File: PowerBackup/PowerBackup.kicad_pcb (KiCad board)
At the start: 4 copper layers, 40 x 41 mm, 3 parts

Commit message: Did some initial board layout
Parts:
- added C1: 1u, Capacitor_SMD:C_0805_2012Metric, F.Cu at (141.8, 115.0)
- added C10: 1u, Capacitor_SMD:C_0805_2012Metric, F.Cu at (125.0, 108.7)
- added C2: 1u, Capacitor_SMD:C_0805_2012Metric, F.Cu at (141.8, 113.0)
- added C3: 1u, Capacitor_SMD:C_0805_2012Metric, F.Cu at (141.8, 110.0)
- added C4: 1u, Capacitor_SMD:C_0805_2012Metric, F.Cu at (141.8, 107.5)
- added C5: 1u, Capacitor_SMD:C_0805_2012Metric, F.Cu at (141.8, 105.0)
- added C6: 1u, Capacitor_SMD:C_0805_2012Metric, F.Cu at (141.8, 102.8)
- added C7: 1u, Capacitor_SMD:C_0805_2012Metric, F.Cu at (141.8, 100.5)
- added C8: 10u, Capacitor_SMD:C_0805_2012Metric, F.Cu at (138.8, 105.5)
- added C9: 4.7u, Capacitor_SMD:C_0805_2012Metric, F.Cu at (136.5, 105.5)
- added D1: MBRB2515L, Package_TO_SOT_SMD:TO-263-2, F.Cu at (134.3, 89.0)
- added D2: MBRB2515L, Package_TO_SOT_SMD:TO-263-2, F.Cu at (119.4, 101.0)
- added J1: Conn_01x02_Female, Connector_JST:JST_XH_B2B-XH-A_1x02_P2.50mm_Vertical, B.Cu at (138.2, 79.8)
- added J2: Conn_01x07_Male, Connector_JST:JST_XH_B7B-XH-A_1x07_P2.50mm_Vertical, F.Cu at (147.6, 100.0)
- added J4: Conn_01x05_Female, Connector_PinHeader_1.00mm:PinHeader_1x05_P1.00mm_Vertical_SMD_Pin1Left, F.Cu at (131.8, 106.4)
- added J6: Conn_01x02_Female, Connector_JST:JST_XH_B2B-XH-A_1x02_P2.50mm_Vertical, F.Cu at (146.5, 92.5)
- added J7: Conn_01x02_Male, Connector_JST:JST_XH_B2B-XH-A_1x02_P2.50mm_Vertical, F.Cu at (114.1, 92.2)
- added Q1: ZXTP25040DFH, Package_TO_SOT_SMD:SOT-23, F.Cu at (137.2, 101.6)
- added R1: 100, Resistor_SMD:R_0805_2012Metric, B.Cu at (144.2, 100.0)
- added R10: 0.001, Resistor_SMD:R_0805_2012Metric, F.Cu at (135.0, 113.2)
- added R11: 0, Resistor_SMD:R_0805_2012Metric, F.Cu at (134.8, 98.8)
- added R12: 1k, Resistor_SMD:R_0805_2012Metric, F.Cu at (133.6, 110.5)
- added R13: 4k7, Resistor_SMD:R_0805_2012Metric, F.Cu at (133.6, 102.8)
- added R14: 200, Resistor_SMD:R_0805_2012Metric, B.Cu at (131.0, 105.6)
- added R15: 4k7, Resistor_SMD:R_0805_2012Metric, F.Cu at (133.6, 100.8)
- added R16: 0, Resistor_SMD:R_0805_2012Metric, F.Cu at (136.4, 96.8)
- added R17: 0, Resistor_SMD:R_0805_2012Metric, F.Cu at (139.8, 95.8)
- added R2: 100, Resistor_SMD:R_0805_2012Metric, B.Cu at (144.4, 104.8)
- added R3: 100, Resistor_SMD:R_0805_2012Metric, B.Cu at (144.4, 109.9)
- added R4: 100, Resistor_SMD:R_0805_2012Metric, B.Cu at (144.4, 115.0)
- added R5: 100, Resistor_SMD:R_0805_2012Metric, B.Cu at (144.4, 107.1)
- added R6: 100, Resistor_SMD:R_0805_2012Metric, B.Cu at (144.4, 102.3)
- added R7: 100, Resistor_SMD:R_0805_2012Metric, B.Cu at (144.4, 112.4)
- added R8: 100, Resistor_SMD:R_0805_2012Metric, F.Cu at (138.2, 98.8)
- added R9: 1k, Resistor_SMD:R_0805_2012Metric, F.Cu at (136.1, 110.5)
- added TH1: Thermistor_NTC, Resistor_SMD:R_0805_2012Metric, F.Cu at (128.8, 108.4)
- added U1: BQ76925RGET, Package_DFN_QFN:HVQFN-24-1EP_4x4mm_P0.5mm_EP2.5x2.5mm, B.Cu at (136.5, 105.2)
- H1, H2, H3: value MountingHole_3.2mm_M3_Pad -> MountingHole_Pad; footprint MountingHole:MountingHole_3.2mm_M3_Pad -> MountingHole:MountingHole_2.7mm_M2.5_Pad
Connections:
- H1 pad 1: (no net) -> GND
- H2 pad 1: (no net) -> GND
- H3 pad 1: (no net) -> GND
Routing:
- net Net-(J3-Pad3): track 0.00 -> 16.6 mm, vias 0 -> 1
- net Net-(C7-Pad1): track 0.00 -> 12.9 mm, vias 0 -> 1
- net Net-(C1-Pad1): track 0.00 -> 12.4 mm, vias 0 -> 1
- net Net-(J5-Pad4): track 0.00 -> 10.9 mm
- net Net-(C2-Pad1): track 0.00 -> 10.9 mm, vias 0 -> 1
- net Net-(J3-Pad4): track 0.00 -> 10.5 mm, vias 0 -> 1
- net Net-(C8-Pad1): track 0.00 -> 9.98 mm, vias 0 -> 1
- net Net-(R11-Pad1): track 0.00 -> 9.76 mm, vias 0 -> 2
- net Net-(C6-Pad1): track 0.00 -> 9.17 mm, vias 0 -> 1
- net Net-(J5-Pad3): track 0.00 -> 8.93 mm
- net Net-(C3-Pad1): track 0.00 -> 8.46 mm, vias 0 -> 1
- net Net-(C5-Pad1): track 0.00 -> 7.85 mm, vias 0 -> 1
- net Net-(J4-Pad2): track 0.00 -> 7.33 mm, vias 0 -> 1
- net Net-(C4-Pad1): track 0.00 -> 6.65 mm, vias 0 -> 1
- net Net-(J4-Pad5): track 0.00 -> 6.32 mm, vias 0 -> 1
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- added copper zone on F.Cu, net +3V3
- added copper zone on F.Cu, net +9V
- added copper zone on F.Cu, net +9VA
- added copper zone on F.Cu, net /Backup/VBAT
- added copper zone on F.Cu, net GND
- added copper zone on In1.Cu, net GND

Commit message: Trying things
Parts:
- added J10: Conn_01x02_Female, Connector_JST:JST_XH_B2B-XH-A_1x02_P2.50mm_Vertical, F.Cu at (116.1, 115.1)
- added J8: Conn_01x02_Female, Connector_JST:JST_XH_B2B-XH-A_1x02_P2.50mm_Vertical, F.Cu at (113.5, 107.9)
- added J9: Conn_01x02_Female, Connector_JST:JST_XH_B2B-XH-A_1x02_P2.50mm_Vertical, F.Cu at (113.5, 91.4)
- D1, D2: value MBRB2515L -> SB2060TA; footprint Package_TO_SOT_SMD:TO-263-2 -> Diode_THT:D_A-405_P5.08mm_Vertical_KathodeUp
- moved C10 24.9 mm to (135.4, 86.1), turned to 0 degrees
- moved D2 19.5 mm to (131.4, 85.6), turned to 180 degrees
- moved J7 18.0 mm to (127.2, 79.8), turned to 0 degrees
- moved D1 5.92 mm to (134.6, 83.1), turned to 0 degrees
- moved J6 2.57 mm to (147.6, 90.2), turned to -90 degrees
- moved J1 1.77 mm to (140.0, 80.0)
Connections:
- D1 pad 1: +9V -> +9VA
- D1 pad 2: +9VA -> +9V
- D2 pad 1: /Backup/VBAT -> +9VA
- D2 pad 2: +9VA -> /Backup/VBAT
- R10 pad 2: GNDD -> GND
- R12 pad 2: GNDD -> GND
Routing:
- net GND: track 3.61 -> 8.52 mm
- net Net-(J2-Pad4): track 0.00 -> 2.51 mm
- net Net-(J2-Pad1): track 0.00 -> 2.48 mm
- net Net-(J5-Pad4): track 10.9 -> 13.4 mm, vias 0 -> 1
- net Net-(J2-Pad2): track 0.20 -> 2.64 mm
- net Net-(J2-Pad3): track 0.00 -> 2.42 mm
- net Net-(J2-Pad5): track 0.03 -> 2.42 mm
- net Net-(J2-Pad6): track 0.03 -> 2.39 mm
- net GNDD: track 2.54 -> 1.39 mm, vias 0 -> 10
- added copper zone on F.Cu, net GNDD
- added copper zone on In2.Cu, net GNDD

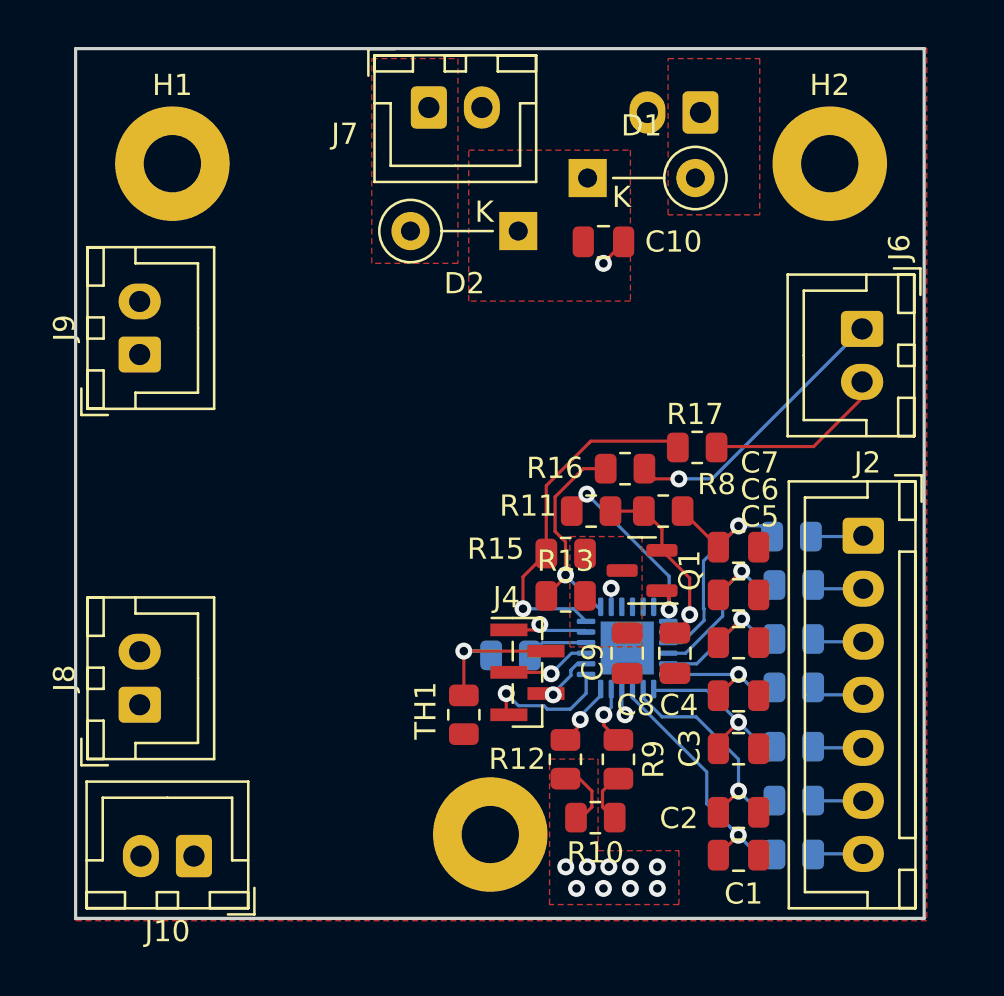
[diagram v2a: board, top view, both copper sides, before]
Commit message: Added 5V 9A buck converter
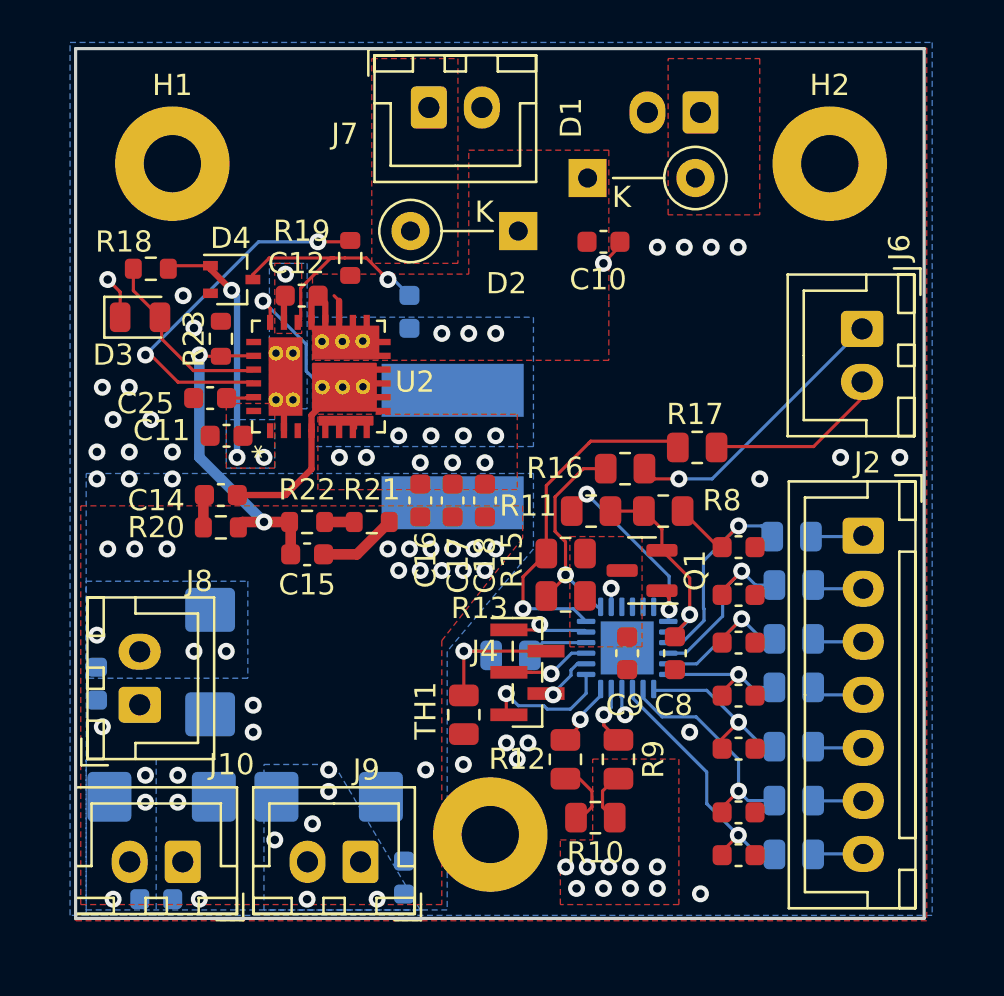
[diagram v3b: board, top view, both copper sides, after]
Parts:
- added C11: 2.2u, Capacitor_SMD:C_0603_1608Metric, F.Cu at (117.6, 95.2)
- added C12: 2.2u, Capacitor_SMD:C_0603_1608Metric, F.Cu at (121.2, 88.6)
- added C13: 0.1u, Capacitor_SMD:C_0603_1608Metric, B.Cu at (126.2, 89.4)
- added C14: 0.1u, Capacitor_SMD:C_0603_1608Metric, F.Cu at (117.3, 98.0)
- added C15: 0.1u, Capacitor_SMD:C_0603_1608Metric, F.Cu at (121.4, 100.8)
- added C16: 0.1u, Capacitor_SMD:C_0603_1608Metric, F.Cu at (126.7, 98.3)
- added C17: 1u, Capacitor_SMD:C_0603_1608Metric, F.Cu at (128.3, 98.3)
- added C18: 50u, Capacitor_SMD:C_0603_1608Metric, F.Cu at (129.8, 98.3)
- added C19: 4.7u, Capacitor_SMD:C_0603_1608Metric, B.Cu at (111.5, 106.9)
- added C20: 4.7u, Capacitor_SMD:C_0603_1608Metric, B.Cu at (114.3, 117.1)
- added C21: 4.7u, Capacitor_SMD:C_0603_1608Metric, B.Cu at (126.0, 116.1)
- added C22: 47u, Capacitor_Tantalum_SMD:CP_EIA-6032-15_Kemet-U, B.Cu at (116.8, 105.9)
- added C23: 47u, Capacitor_Tantalum_SMD:CP_EIA-6032-15_Kemet-U, B.Cu at (114.6, 112.3)
- added C24: 47u, Capacitor_Tantalum_SMD:CP_EIA-6032-15_Kemet-U, B.Cu at (122.4, 112.3)
- added C25: 2.2u, Capacitor_SMD:C_0603_1608Metric, F.Cu at (116.8, 93.5)
- added D3: LED_Small, LED_SMD:LED_0805_2012Metric, F.Cu at (113.5, 89.7)
- added D4: BAT54W, Package_TO_SOT_SMD:SOT-323_SC-70, F.Cu at (117.9, 87.9)
- added L1: 3.3u, Backup:Inductor_EXL1V0707-3R3-R, B.Cu at (128.3, 95.8)
- added R18: 1.5k, Resistor_SMD:R_0603_1608Metric, F.Cu at (114.0, 87.4)
- added R19: 10k, Resistor_SMD:R_0603_1608Metric, F.Cu at (123.4, 86.9)
- added R20: 19.6k, Resistor_SMD:R_0603_1608Metric, F.Cu at (117.3, 99.6)
- added R21: 7k5, Resistor_SMD:R_0603_1608Metric, F.Cu at (124.5, 99.3)
- added R22: 150k, Resistor_SMD:R_0603_1608Metric, F.Cu at (121.4, 99.3)
- added R23: 30k, Resistor_SMD:R_0603_1608Metric, F.Cu at (117.3, 90.7)
- added U2: MIC26903, Backup:MIC26903YJL-TR, F.Cu at (121.9, 92.5)
- C1, C10, C2, C3, C4, C5, C6, C7, C8, C9: footprint Capacitor_SMD:C_0805_2012Metric -> Capacitor_SMD:C_0603_1608Metric
- moved J9 26.1 mm to (123.9, 115.3), turned to 180 degrees
- moved J10 0.59 mm to (115.5, 115.3)
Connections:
- C1 pad 2: GND -> GNDS
- C10 pad 2: GNDD -> GND
- C2 pad 2: GND -> GNDS
- C3 pad 2: GND -> GNDS
- C4 pad 2: GND -> GNDS
- C5 pad 2: GND -> GNDS
- C6 pad 2: GND -> GNDS
- C7 pad 2: GND -> GNDS
- C8 pad 2: GND -> GNDS
- C9 pad 2: GND -> GNDS
- J10 pad 1: unconnected-(J10-Pad1) -> +5V
- J10 pad 2: unconnected-(J10-Pad2) -> GND
- J7 pad 2: GNDD -> GND
- J8 pad 1: unconnected-(J8-Pad1) -> +5V
- J8 pad 2: unconnected-(J8-Pad2) -> GND
- J9 pad 1: unconnected-(J9-Pad1) -> +5V
- J9 pad 2: unconnected-(J9-Pad2) -> GND
- R10 pad 2: GND -> GNDS
- R12 pad 2: GND -> GNDS
- TH1 pad 2: GND -> GNDS
- U1 pad 10: GND -> GNDS
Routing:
- net Net-(R19-Pad2): track 0.00 -> 17.5 mm, vias 0 -> 2
- net Net-(C15-Pad2): track 0.00 -> 15.9 mm, vias 0 -> 2
- net /Backup/SW: track 0.00 -> 15.0 mm, vias 0 -> 8
- net Net-(C13-Pad1): track 0.00 -> 12.5 mm, vias 0 -> 1
- net /Backup/PVDD: track 0.00 -> 11.6 mm, vias 0 -> 3
- net Net-(D3-Pad2): track 0.00 -> 8.63 mm
- net GND: track 8.52 -> 14.0 mm, vias 1 -> 27
- net +9VA: track 0.00 -> 4.14 mm
- net GNDS: track 0.00 -> 3.78 mm, vias 0 -> 26
- net +5V: track 0.00 -> 3.73 mm, vias 0 -> 23
- net Net-(U2-Pad27): track 0.00 -> 1.63 mm
- net Net-(C14-Pad2): track 0.00 -> 1.54 mm
- net Net-(R21-Pad2): track 0.00 -> 1.40 mm
- net GNDD: track 1.39 -> 0.00 mm, vias 10 -> 0
- added copper zone on B.Cu, net +5V
- added copper zone on F.Cu, net +5V
- added copper zone on B.Cu, net /Backup/PVDD
- added copper zone on F.Cu, net /Backup/PVDD
- added copper zone on B.Cu, net /Backup/SW
- added copper zone on B.Cu, net GND
- added copper zone on B.Cu, net GNDS
- added copper zone on F.Cu, net GNDS
- added copper zone on In2.Cu, net GNDS
- removed copper zone on F.Cu, net GNDD
- removed copper zone on In2.Cu, net GNDD

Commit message: Looking over desing
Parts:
- added J3: Conn_01x04_Male, Connector_JST:JST_SH_BM04B-SRSS-TB_1x04-1MP_P1.00mm_Vertical, B.Cu at (139.1, 92.1)
- added J5: Conn_01x04_Male, Connector_JST:JST_SH_BM04B-SRSS-TB_1x04-1MP_P1.00mm_Vertical, B.Cu at (144.6, 92.1)
- C18: value 50u -> 47u; footprint Capacitor_SMD:C_0603_1608Metric -> Capacitor_Tantalum_SMD:CP_EIA-6032-15_Kemet-U
- R20: value 19.6k -> 10k
- moved R16 6.84 mm to (142.1, 93.0)
- moved R17 5.40 mm to (142.1, 90.9)
- moved C18 3.21 mm to (126.6, 98.6)
- moved J6 2.91 mm to (148.3, 93.0), turned to 90 degrees
- moved C16 2.25 mm to (129.0, 98.3)
- moved C17 2.23 mm to (130.5, 98.3)
- moved R21 1.18 mm to (123.5, 100.0), turned to 90 degrees
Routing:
- net +3V3: track 0.88 -> 25.8 mm, vias 1 -> 4
- net Net-(J3-Pad4): track 10.5 -> 23.6 mm, vias 1 -> 2
- net Net-(J5-Pad4): track 13.4 -> 5.80 mm
- net Net-(J3-Pad3): track 17.1 -> 21.8 mm, vias 1 -> 3
- net +5V: track 3.73 -> 0.00 mm, vias 23 -> 21
- net Net-(Q1-Pad1): track 9.76 -> 11.5 mm, vias 2 -> 3
- net +9VA: track 4.14 -> 5.84 mm
- net /Backup/SW: track 15.0 -> 16.7 mm, vias 8 -> 10
- net Net-(J5-Pad3): track 8.60 -> 7.19 mm, vias 0 -> 1
- net GNDS: vias 26 -> 32
- net GND: vias 27 -> 29
- added copper zone on B.Cu, net +9VA
- added copper zone on F.Cu, net /Backup/SW
